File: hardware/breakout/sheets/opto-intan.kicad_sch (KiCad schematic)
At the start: 33 parts, among them J46 Intan opto out: EVT_STROBE_IN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, J47 Intan opto out: BARCODE_INTAN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, J48 Intan opto out: RWD_CMD_INTAN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, J49 Intan opto out: RWD_DLVR_INTA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, J50 Intan opto out: STIM_TRIG_INT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, J51 Intan RHS stim status in (BNC), U63 LD1117S50TR_SOT223, U64 ACSL-6400-00TE, U65 ACSL-6420-00TE

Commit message: fix(hw): drop opto-intan's pull-ups to 3.9k, within ACSL-6400/6420's own RL-max
Same datasheet violation fix round 1 corrected on opto-ni.kicad_sch (RL-max =
4k, Broadcom AV02-0235EN's own "Recommended Operating Conditions"), found
here independently rather than inferred from that sibling sheet: the
datasheet is ONE table covering the whole ACSL-6xx0 family (ACSL-6210
through ACSL-6420) with no per-device split, and the output stage RL-max
characterizes is schematically identical across every family member and
channel -- so the 4k ceiling binds ACSL-6420's own VO1-VO4 pins exactly as
it binds ACSL-6400's, on both this sheet's own packages. 3.9k (E24) is the
largest standard value at or under that limit.

NI-side's 250mA connector budget argument does not transfer here and is not
reused: this sheet's output side runs from the board's own isolated ISO_5V
rail, not NI's connector, so there is no 250mA ceiling. The reason to move
off 10k is purely that a datasheet maximum is a datasheet maximum.

A from-scratch ISO_5V/ISO_P12 budget check (not assumed to inherit opto-ni's
own numbers, which are computed against a different rail with a different
channel mix) found the fix's own marginal cost trivial: the 6 ISO_5V-
referenced pull-ups add ~4.7mA (7.7mA at 3.9k vs 3.0mA at 10k) against a
rail whose other loads (6 channels' worth of detector supply current plus
2 LED forward currents) already run ~80-85mA worst case, reaching ISO_P12
alongside mux-intan's own 8 INA105KUs (~16mA) on the shared, 150mA-rated
TPS7A4901 -- ~34-49mA of headroom either way.

gen_breakout_opto_intan.py and check_breakout_opto_intan_netlist.py both
move to 3.9k; opto-intan.kicad_sch regenerated (8 pull-ups). hardware/
README.md's Opto-Intan section gains the same pull-up writeup Opto-NI's own
already carries. The checker's own two pull-up drift negative controls still
fire -- one now specifically targets the stale 10k value (the most
meaningful regression this fix guards against), the other the mule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
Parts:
- R172, R174, R176, R178, R180, R182, R184, R186: value 10k -> 3.9k
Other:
- note added: "NI's 250mA budget does NOT apply here (this sheet runs off the board's own"
- note added: "current). PULL-UPS: 3.9k throughout -- FIX ROUND 2: ACSL-6400/ACSL-6420 share ONE"
- note added: "datasheet RL-max (4k, Broadcom AV02-0235EN's family-wide table), which the"
- note added: "isolated ISO_5V rail); ISO_5V/ISO_P12's own budget was checked from scratch --"
- note added: "original 10k exceeded (same violation fix round 1 corrected on opto-ni.kicad_sch)."
- note added: "~34-49mA of headroom against the shared TPS7A4901's 150mA cap either way."
- note removed: "current). PULL-UPS: 10k throughout (this task's own NI-side instruction, applied"
- note removed: "here too for consistency and because the ISO domain's own 2W power budget,"
- note removed: "shared with 8 Intan difference amplifiers, is tighter than NI's 250mA/connector)."

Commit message: fix(hw): one optocoupler LED per driver pin
The _BUF bank names 19 signals for what is really a 30-LED board. The 11
unnamed LEDs got doubled onto pins that already had one, and put +5V on
two sync-module GPIOs.

(a) Doubled loads. Each ACSL-6400/6420 LED draws ~7.33mA from +5V through
430R -- a value pinned between the part's 7-15mA recommended band and its
7.0mA worst-case switching threshold, so it cannot be lowered to suit a
driver. EVT_STROBE_BUF, RWD_CMD_BUF and STIM_TRIG_BUF each fed an NI LED
and an Intan LED from one HCT541 output (14.7mA vs 6mA IOL); BARCODE_PI
did the same off the pi-interface trigger buffer; and bare RWD_DLVR fed
both of its optocouplers straight off the 74HCT32 reward-OR gate, 14.7mA
against 4mA. That last one is the one with a failure mode rather than a
margin: RWD_DLVR's LOW is read by U14 (SN74LVC541APW, V_IL,max 0.8V), and
an HCT gate's VOL at 3.7x its rated sink plausibly exceeds it -- leaving
RWD_DLVR_PI stuck HIGH, the sync module recording reward-delivered
continuously. Same failure signature as the reward-OR polarity defect
caught on this board at task 8 fix round 1.

U10's 5 spare channels now carry EVT_STROBE_INTAN_BUF, RWD_CMD_INTAN_BUF,
STIM_TRIG_INTAN_BUF, RWD_DLVR_BUF and RWD_DLVR_INTAN_BUF (8 of 8 used);
U15's carry BARCODE_BUF and BARCODE_INTAN_BUF. The *_INTAN_BUF legs tap
the same *_CLAMP node their NI twin taps -- the established fan-out
point, one protection network with N buffered copies. RWD_DLVR and
BARCODE_PI now drive only CMOS inputs and panel headers.

(b) +5V reaching GPIO20/21 through an optocoupler LED. R166/R168 (430R
from +5V) fed ACSL-6400 LEDs whose cathodes sat on PD1_COMP/PD2_COMP --
which wire DIRECTLY into the sync module's GPIO20/21. With the LED off
that node idles ~3.6-3.8V, above the 3.3V rail and held only by the
module's ESD clamp; with this board powered and the sync box off, ~7mA is
injected into an unpowered pad. These were the only 2 of 24 NI
optocoupler LEDs not driven from a buffered le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
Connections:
- net BARCODE_PI renamed BARCODE_INTAN_BUF
- net EVT_STROBE_BUF renamed EVT_STROBE_INTAN_BUF
- net RWD_CMD_BUF renamed RWD_CMD_INTAN_BUF
- net RWD_DLVR renamed RWD_DLVR_INTAN_BUF
- net STIM_TRIG_BUF renamed STIM_TRIG_INTAN_BUF

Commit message: fix(hardware): drive the optocoupler LEDs (F1, both halves)
430R never switched these LEDs. The original sizing solved
(5.0 - V_OL - V_F)/I correctly but against the rail's NOMINAL 5.00V and
V_F TYP; +5V reaches the anodes through F4 and D3 (0.42-0.49V of drop)
and V_F's worst case is 1.80V, so the real worst-case current was ~5mA
against the ACSL-6xx0's 7.0mA I_FH minimum. 30 channels were not
guaranteed to switch for seventy-three commits.

Both halves land together because neither is shippable alone -- 430R
starves the LED, and 249R (~12.7mA) overloads a single 7.5mA output.

Resistors, rail-aware: 430R -> 249R on the 30 LEDs fed from +5V, ->
301R on the 2 fed from ISO_5V. ISO_5V is regulated locally with nothing
in series, so 249R there would give 15.1mA -- past the 15mA ABSOLUTE
maximum. One value is wrong on one rail or the other.

Paralleling: every buffer-driven LED now has two SN74AHCT541 outputs
from tied inputs. Four new packages (U70-U73) plus C151-C154, 5 buffer
packages to 9, 6 spare channels. Channel maps are mirrored from the
tables that built the first leg rather than re-listed, so the legs
cannot drift apart. Refdes minted out of band, above the board maximum:
8 refs added, 0 removed, 0 renumbered.

This also fixes a per-PACKAGE limit no per-pin check could see. The
AHCT541's GND absolute maximum is 75mA (SCLS269Q 4.1, not the 100mA
hardware/README.md claimed); U8/U9 drive eight LEDs each; the drive is
active-low and the event bus idles at 0x0000, so sixteen LEDs are lit
CONTINUOUSLY. At 249R unparalleled that is ~101mA through one ground
pin. Paralleled it is 55.6mA worst case.

RHS_STIM_OUT's LED moves to a new buffered leg (RHS_STIM_OUT_BUF, off
U11's last two spare channels). It was the one channel driven by an
ACSL-6420 output rather than a buffer -- a deliberate, checked exception
that was correct at 430R (8.61mA of a 13mA budget) and not correct at
249R (13.85mA with its pull-up). The exception did not change; the
number it had been checked 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
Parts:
- R171, R173, R175, R177, R179, R181: value 430 -> 249
- R183, R185: value 430 -> 301
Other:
- note added: "LED DRIVE: 249R on +5V, 301R on ISO_5V (E96, 1%) -- FINDING F1, 2026-08-16. Was a"
- note added: "PULL-UPS: 3.9k throughout -- FIX ROUND 2: ACSL-6400/ACSL-6420 share ONE"
- note added: "TWO paralleled buffer outputs (F1b); the two ISO_5V LEDs have no board driver."
- note added: "drop) while ISO_5V is regulated locally with nothing in series, so 249R there"
- note added: "minimum). This is the only sheet with LEDs on BOTH rails, so it is the only one"
- note added: "single 430R, which under-drove every LED (~5mA worst case against a 7.0mA I_FH"
- note added: "where one value is actually wrong: +5V arrives through F4 and D3 (0.38-0.45V of"
- note added: "would give 15.1mA -- past the 15mA ABSOLUTE maximum. Each +5V LED is driven by"
- note removed: "LED DRIVE: 430R (same value/derivation as opto-ni.kicad_sch -- ~7.33mA, roughly"
- note removed: "current). PULL-UPS: 3.9k throughout -- FIX ROUND 2: ACSL-6400/ACSL-6420 share ONE"
- note removed: "half the ACSL-6xx0 family's shared datasheet-recommended top-of-range forward"

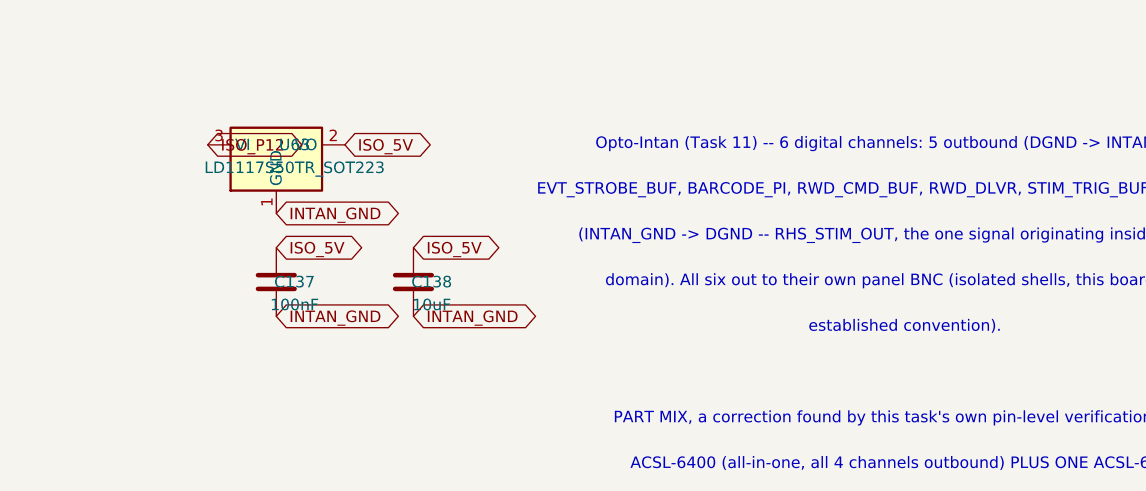
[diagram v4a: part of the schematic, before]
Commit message: fix(hardware): take the ISO_5V branch off the isolated module (F5, on a regulated part)
ISO_5V was made by a linear regulator off ISO_P12. A linear regulator
passes its output current straight to its input, so this sheet's whole
63-91 mA digital branch -- six detector stages, six pull-ups, two inbound
LEDs -- was drawn THROUGH the isolated +-12 V module. Re-derived from the
netlist after finding F1 (which raised the two ISO_5V LEDs from 7.33 mA to
~10.5 mA each), ISO_P12 sat at 114% typ / 170% max of the IH1215D's 66 mA
per-rail rating while ISO_N12 carried 12-16 mA.

Two defects in one. The over-rating, and an imbalance large enough that the
module's own +-5% cross-regulation figure -- characterised only with the
lighter rail at 25-100% -- did not describe this board at all. Both rails
now carry 12-16 mA and match. It also retires 0.37-0.58 W of LDO
dissipation inside a sealed 2U chassis.

NOT THE TMA-0505S THE AUDIT NAMED.

The audit picked that part because it is already on the board (U62, the DNP
NI-side fallback) and so costs no new part number. The handoff required
pinning it in datasheet-params.toml before the recommendation could be
final, and pinning it is exactly what killed it: THE TMA SERIES IS
UNREGULATED. ISO_5V would sit at 31-46% of its rating, and an unregulated
module's output rises at light load -- the audit itself records the IH1215D
doing +10% at ~20%. At +10% ISO_5V reaches 5.50 V, EXACTLY the ACSL-6xx0's
VDD absolute maximum with zero headroom, and it would drive finding F1's
freshly-sized 301 ohm ISO_5V resistors to 14.3 mA against a 15 mA absolute
maximum. Fixing F5 that way would have broken F1.

Shipped on a TMR 1-0511 instead: Traco's regulated 1 W sibling, +-1% set
accuracy, 0.2% line, 0.5% load, so ISO_5V stays 5.0 V and both problems
disappear. Also 1500 VDC isolation rather than 1000, no minimum load, 76%
efficient rather than 71%, SIP-6 through-hole and hand-solderable. Cost:
one new part number -- the only one this audit implementat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
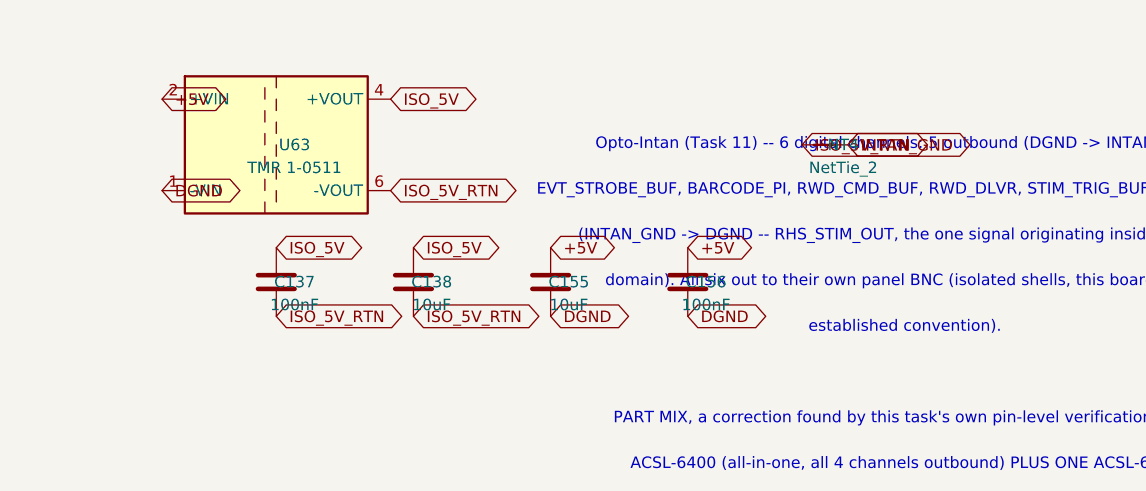
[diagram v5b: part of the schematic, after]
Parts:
- removed U63: LD1117S50TR_SOT223, Package_TO_SOT_SMD:SOT-223-3_TabPin2, symbol Regulator_Linear:LD1117S50TR_SOT223
- added C155: 10uF, Capacitor_SMD:C_1206_3216Metric, symbol Device:C
- added C156: 100nF, Capacitor_SMD:C_0603_1608Metric, symbol Device:C
- added NT4: NetTie_2, NetTie:NetTie-2_SMD_Pad2.0mm, symbol Device:NetTie_2
- added U63: TMR 1-0511, Converter_DCDC:Converter_DCDC_TRACO_TMR-1-xxxx_Single_THT, symbol Converter_DCDC_Isolated:TMR_1-0511
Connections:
- net +5V: now also C155.1, C156.1, U63.2 (+VIN)
- net DGND: now also C155.2, C156.2, U63.1 (-VIN)
- net INTAN_GND: now also NT4.2; no longer C137.2, C138.2
- net ISO_5V: now also U63.4 (+VOUT)
- new net ISO_5V_RTN: C137.2, C138.2, NT4.1, U63.6 (-VOUT)
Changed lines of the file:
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@@
 	(paper "A2")
 	(symbol
-		(lib_id "Regulator_Linear:LD1117S50TR_SOT223")
+		(lib_id "Converter_DCDC_Isolated:TMR_1-0511")
 		(at 299.72 20.32 0)
 		(unit 1)
@@
 			(effects (font (size 1.27 1.27)))
 		)
-		(property "Value" "LD1117S50TR_SOT223"
+		(property "Value" "TMR 1-0511"
 			(at 301.752 22.86 0)
 			(effects (font (size 1.27 1.27)))
 		)
-		(property "Footprint" "Package_TO_SOT_SMD:SOT-223-3_TabPin2"
+		(property "Footprint" "Converter_DCDC:Converter_DCDC_TRACO_TMR-1-xxxx_Single_THT"
 			(at 299.72 20.32 0)
 			(effects (font (size 1.27 1.27)) (hide yes))
@@
 		(pin "1")
 		(pin "2")
-		(pin "3")
+		(pin "4")
+		(pin "6")
 		(instances
 			(project "breakout"
@@
 		)
 	)
-	(global_label "ISO_P12"
-		(shape bidirectional)
-		(at 292.1 20.32 0)
-		(effects (font (size 1.27 1.27)) (justify left))
-		(property "Intersheetrefs" "${INTERSHEET_REFS}"
-			(at 292.1 20.32 0)
+	(global_label "+5V"
+		(shape bidirectional)
+		(at 287.02000000000004 15.24 0)
+		(effects (font (size 1.27 1.27)) (justify left))
+		(property "Intersheetrefs" "${INTERSHEET_REFS}"
+			(at 287.02000000000004 15.24 0)
+			(effects (font (size 1.27 1.27)) (hide yes))
+		)
+	)
+	(global_label "DGND"
+		(shape bidirectional)
+		(at 287.02000000000004 25.4 0)
+		(effects (font (size 1.27 1.27)) (justify left))
+		(property "Intersheetrefs" "${INTERSHEET_REFS}"
+			(at 287.02000000000004 25.4 0)
+			(effects (font (size 1.27 1.27)) (hide yes))
+		)
+	)
+	(global_label "ISO_5V"
+		(shape bidirectional)
+		(at 312.42 15.24 0)
+		(effects (font (size 1.27 1.27)) (justify left))
+		(property "Intersheetrefs" "${INTERSHEET_REFS}"
+			(at 312.42 15.24 0)
+			(effects (font (size 1.27 1.27)) (hide yes))
+		)
+	)
+	(global_label "ISO_5V_RTN"
+		(shape bidirectional)
+		(at 312.42 25.4 0)
+		(effects (font (size 1.27 1.27)) (justify left))
+		(property "Intersheetrefs" "${INTERSHEET_REFS}"
+			(at 312.42 25.4 0)
+			(effects (font (size 1.27 1.27)) (hide yes))
+		)
+	)
+	(symbol
+		(lib_id "Device:NetTie_2")
+		(at 360.68 20.32 0)
+		(unit 1)
+		(exclude_from_sim no)
+		(in_bom yes)
+		(on_board yes)
+		(dnp no)
+		(property "Reference" "NT4"
+			(at 362.712 20.32 0)
+			(effects (font (size 1.27 1.27)))
+		)
+		(property "Value" "NetTie_2"
+			(at 362.712 22.86 0)
+			(effects (font (size 1.27 1.27)))
+		)
+		(property "Footprint" "NetTie:NetTie-2_SMD_Pad2.0mm"
+			(at 360.68 20.32 0)
+			(effects (font (size 1.27 1.27)) (hide yes))
+		)
+		(property "Datasheet" ""
+			(at 360.68 20.32 0)
+			(effects (font (size 1.27 1.27)) (hide yes))
+		)
+		(pin "1")
+		(pin "2")
+		(instances
+			(project "breakout"
+				(path "/d2c4d978-5db4-46d9-a1cd-a7af0aeb1700/34211e85-eb6f-485e-95d9-0458e705752e"
+					(reference "NT4") (unit 1)
+				)
+			)
+		)
+	)
+	(global_label "ISO_5V_RTN"
+		(shape bidirectional)
+		(at 358.14 20.32 0)
+		(effects (font (size 1.27 1.27)) (justify left))
+		(property "Intersheetrefs" "${INTERSHEET_REFS}"
+			(at 358.14 20.32 0)
 			(effects (font (size 1.27 1.27)) (hide yes))
 		)
@@
 	(global_label "INTAN_GND"
 		(shape bidirectional)
-		(at 299.72 27.94 0)
-		(effects (font (size 1.27 1.27)) (justify left))
-		(property "Intersheetrefs" "${INTERSHEET_REFS}"
-			(at 299.72 27.94 0)
-			(effects (font (size 1.27 1.27)) (hide yes))
-		)
-	)
-	(global_label "ISO_5V"
-		(shape bidirectional)
-		(at 307.34000000000003 20.32 0)
-		(effects (font (size 1.27 1.27)) (justify left))
-		(property "Intersheetrefs" "${INTERSHEET_REFS}"
-			(at 307.34000000000003 20.32 0)
+		(at 363.22 20.32 0)
+		(effects (font (size 1.27 1.27)) (justify left))
+		(property "Intersheetrefs" "${INTERSHEET_REFS}"
+			(at 363.22 20.32 0)
 			(effects (font (size 1.27 1.27)) (hide yes))
 		)
@@
 		)
 	)
-	(global_label "INTAN_GND"
+	(global_label "ISO_5V_RTN"
 		(shape bidirectional)
 		(at 299.72 39.370000000000005 0)
@@
 		)
 	)
-	(global_label "INTAN_GND"
+	(global_label "ISO_5V_RTN"
 		(shape bidirectional)
 		(at 314.96000000000004 39.370000000000005 0)
@@
 			(effects (font (size 1.27 1.27)) (hide yes))
 		)
+	)
+	(symbol
+		(lib_id "Device:C")
+		(at 330.20000000000005 35.56 0)
+		(unit 1)
+		(exclude_from_sim no)
+		(in_bom yes)
+		(on_board yes)
+		(dnp no)
+		(property "Reference" "C155"
+			(at 332.232 35.56 0)
+			(effects (font (size 1.27 1.27)))
+		)
+		(property "Value" "10uF"
+			(at 332.232 38.1 0)
+			(effects (font (size 1.27 1.27)))
+		)
+		(property "Footprint" "Capacitor_SMD:C_1206_3216Metric"
+			(at 330.20000000000005 35.56 0)
+			(effects (font (size 1.27 1.27)) (hide yes))
+		)
+		(property "Datasheet" ""
+			(at 330.20000000000005 35.56 0)
+			(effects (font (size 1.27 1.27)) (hide yes))
+		)
+		(pin "1")
+		(pin "2")
+		(instances
+			(project "breakout"
+				(path "/d2c4d978-5db4-46d9-a1cd-a7af0aeb1700/34211e85-eb6f-485e-95d9-0458e705752e"
+					(reference "C155") (unit 1)
+				)
+			)
+		)
+	)
+	(global_label "+5V"
+		(shape bidirectional)
+		(at 330.20000000000005 31.750000000000004 0)
+		(effects (font (size 1.27 1.27)) (justify left))
+		(property "Intersheetrefs" "${INTERSHEET_REFS}"
+			(at 330.20000000000005 31.750000000000004 0)
+			(effects (font (size 1.27 1.27)) (hide yes))
+		)
+	)
+	(global_label "DGND"
+		(shape bidirectional)
+		(at 330.20000000000005 39.370000000000005 0)
+		(effects (font (size 1.27 1.27)) (justify left))
+		(property "Intersheetrefs" "${INTERSHEET_REFS}"
+			(at 330.20000000000005 39.370000000000005 0)
+			(effects (font (size 1.27 1.27)) (hide yes))
+		)
+	)
+	(symbol
+		(lib_id "Device:C")
+		(at 345.44000000000005 35.56 0)
+		(unit 1)
+		(exclude_from_sim no)
+		(in_bom yes)
+		(on_board yes)
+		(dnp no)
+		(property "Reference" "C156"
+			(at 347.47200000000004 35.56 0)
+			(effects (font (size 1.27 1.27)))
+		)
+		(property "Value" "100nF"
+			(at 347.47200000000004 38.1 0)
+			(effects (font (size 1.27 1.27)))
+		)
+		(property "Footprint" "Capacitor_SMD:C_0603_1608Metric"
+			(at 345.44000000000005 35.56 0)
+			(effects (font (size 1.27 1.27)) (hide yes))
+		)
+		(property "Datasheet" ""
+			(at 345.44000000000005 35.56 0)
+			(effects (font (size 1.27 1.27)) (hide yes))
+		)
+		(pin "1")
+		(pin "2")
+		(instances
+			(project "breakout"
+				(path "/d2c4d978-5db4-46d9-a1cd-a7af0aeb1700/34211e85-eb6f-485e-95d9-0458e705752e"
+					(reference "C156") (unit 1)
+				)
+			)
+		)
+	)
+	(global_label "+5V"
+		(shape bidirectional)
+		(at 345.44000000000005 31.750000000000004 0)
+		(effects (font (size 1.27 1.27)) (justify left))
+		(property "Intersheetrefs" "${INTERSHEET_REFS}"
+			(at 345.44000000000005 31.750000000000004 0)
+			(effects (font (size 1.27 1.27)) (hide yes))
+		)
+	)
+	(global_label "DGND"
+		(shape bidirectional)
+		(at 345.44000000000005 39.370000000000005 0)
+		(effects (font (size 1.27 1.27)) (justify left))
+		(property "Intersheetrefs" "${INTERSHEET_REFS}"
+			(at 345.44000000000005 39.370000000000005 0)
+			(effects (font (size 1.27 1.27)) (hide yes))
+		)
